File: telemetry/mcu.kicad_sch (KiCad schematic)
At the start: 2 parts, among them J7 CN7, J9 CN10

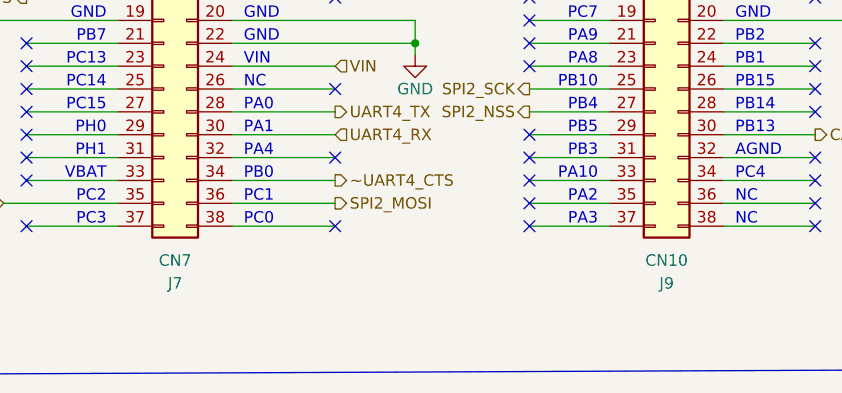
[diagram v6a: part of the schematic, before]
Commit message: fix(telemetry): corrected some ERC issues
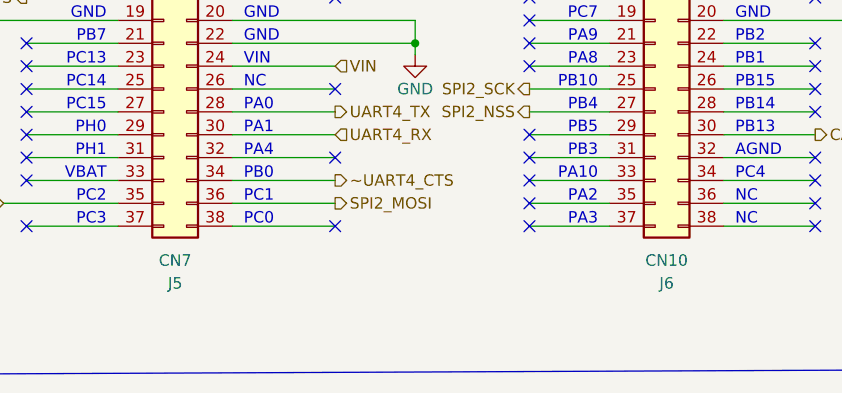
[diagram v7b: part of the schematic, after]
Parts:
- renumbered J7 to J5, J9 to J6
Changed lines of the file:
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@@
   (title_block
     (title "On-Car Telemetry")
-    (date "2023-03-31")
+    (date "2023-04-04")
     (rev "1.0.0")
     (company "SUFST - Southampton University Formula Student Team")
     (comment 1 "STAG 9")
-    (comment 2 "Esteban Norena")
+    (comment 2 "Esteban Norena, Tim Brewis")
     (comment 3 "Tim Brewis")
   )
@@
   (symbol (lib_id "power:GND") (at 143.51 87.63 0) (unit 1)
     (in_bom yes) (on_board yes)
-    (property "Reference" "#PWR0114" (id 0) (at 143.51 93.98 0)
+    (property "Reference" "#PWR022" (id 0) (at 143.51 93.98 0)
       (effects (font (size 1.27 1.27)) hide)
     )
@@
   (symbol (lib_id "power:GND") (at 90.17 85.09 0) (unit 1)
     (in_bom yes) (on_board yes)
-    (property "Reference" "#PWR0115" (id 0) (at 90.17 91.44 0)
+    (property "Reference" "#PWR020" (id 0) (at 90.17 91.44 0)
       (effects (font (size 1.27 1.27)) hide)
     )
@@
   (symbol (lib_id "power:GND") (at 139.7 69.85 0) (unit 1)
     (in_bom yes) (on_board yes)
-    (property "Reference" "#PWR0113" (id 0) (at 139.7 76.2 0)
+    (property "Reference" "#PWR021" (id 0) (at 139.7 76.2 0)
       (effects (font (size 1.27 1.27)) hide)
     )
@@
   (symbol (lib_id "power:GND") (at 195.58 86.36 0) (unit 1)
     (in_bom yes) (on_board yes)
-    (property "Reference" "#PWR0112" (id 0) (at 195.58 92.71 0)
+    (property "Reference" "#PWR023" (id 0) (at 195.58 92.71 0)
       (effects (font (size 1.27 1.27)) hide)
     )
@@
   (symbol (lib_id "Connector_Generic:Conn_02x19_Odd_Even") (at 170.18 83.82 0) (unit 1)
     (in_bom yes) (on_board yes)
-    (property "Reference" "J9" (id 0) (at 171.45 113.03 0))
+    (property "Reference" "J6" (id 0) (at 171.45 113.03 0))
     (property "Value" "CN10" (id 1) (at 171.45 110.49 0))
     (property "Footprint" "SUFST:NUCLEO-F446RE-2x19-CON" (id 2) (at 170.18 83.82 0)
@@
   (symbol (lib_id "Connector_Generic:Conn_02x19_Odd_Even") (at 115.57 83.82 0) (unit 1)
     (in_bom yes) (on_board yes)
-    (property "Reference" "J7" (id 0) (at 116.84 113.03 0))
+    (property "Reference" "J5" (id 0) (at 116.84 113.03 0))
     (property "Value" "CN7" (id 1) (at 116.84 110.49 0))
     (property "Footprint" "SUFST:NUCLEO-F446RE-2x19-CON" (id 2) (at 115.57 83.82 0)

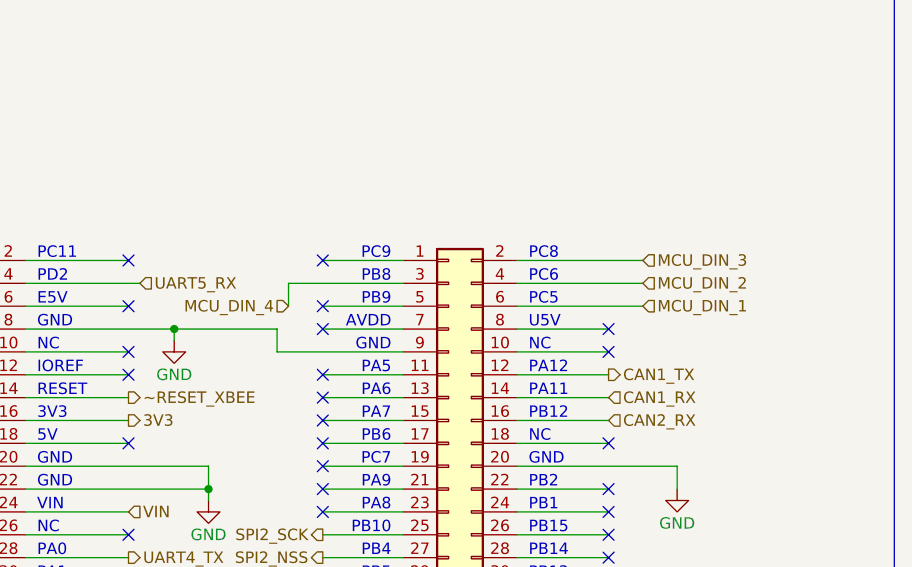
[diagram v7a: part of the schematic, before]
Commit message: feat(telemetry): completed layout
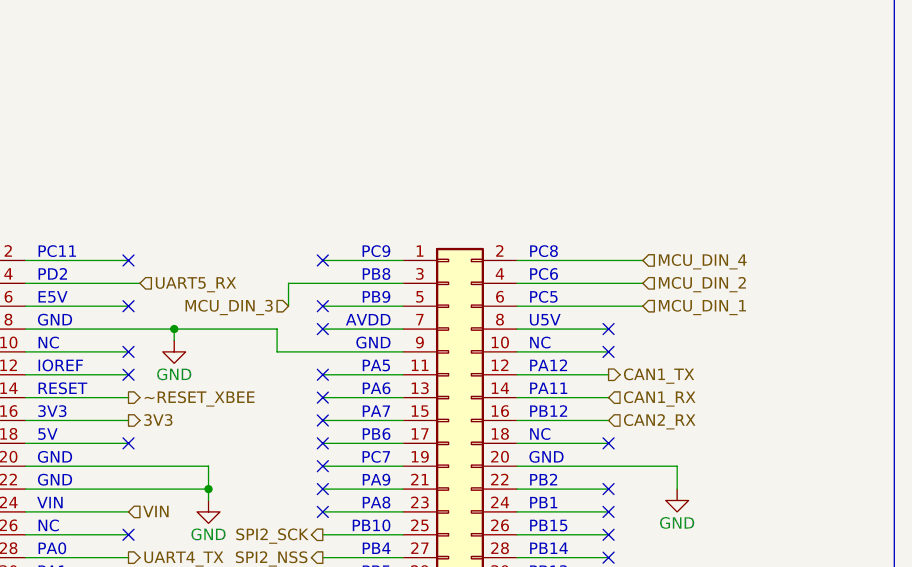
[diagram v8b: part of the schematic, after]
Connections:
- net MCU_DIN_3: now also J6.3 (Pin_3); no longer J6.2 (Pin_2)
- net MCU_DIN_4: now also J6.2 (Pin_2); no longer J6.3 (Pin_3)
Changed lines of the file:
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@@
     (effects (font (size 1.27 1.27)) (justify right))
   )
-  (hierarchical_label "MCU_DIN_3" (shape input) (at 191.77 60.96 0)
-    (effects (font (size 1.27 1.27)) (justify left))
+  (hierarchical_label "MCU_DIN_3" (shape input) (at 152.4 66.04 180)
+    (effects (font (size 1.27 1.27)) (justify right))
   )
   (hierarchical_label "UART4_RX" (shape input) (at 134.62 96.52 0)
@@
     (effects (font (size 1.27 1.27)) (justify left))
   )
-  (hierarchical_label "MCU_DIN_4" (shape input) (at 152.4 66.04 180)
-    (effects (font (size 1.27 1.27)) (justify right))
+  (hierarchical_label "MCU_DIN_4" (shape input) (at 191.77 60.96 0)
+    (effects (font (size 1.27 1.27)) (justify left))
   )
   (hierarchical_label "~RESET_XBEE" (shape output) (at 134.62 76.2 0)
